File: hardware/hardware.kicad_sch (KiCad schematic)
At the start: 34 parts, among them J2 Conn_01x03, Q1 AON6500, Q2 AON6500, Q3 AON6500, Q4 AON6500, Q5 AON6500, Q6 AON6500, U1 CH32M007G8R6

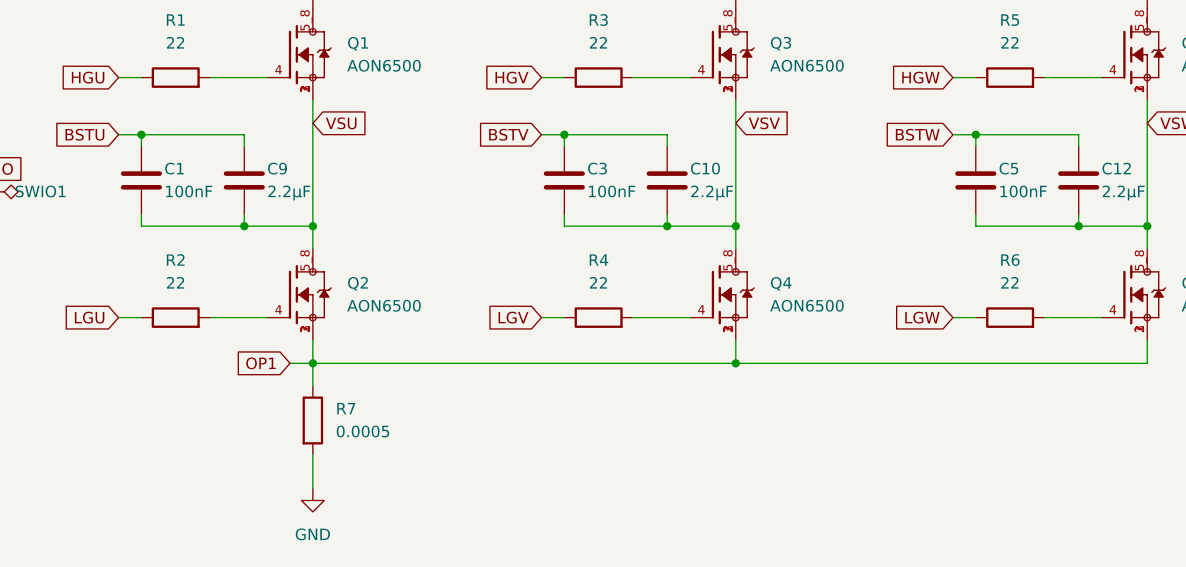
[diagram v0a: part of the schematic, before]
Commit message: change gate resistors
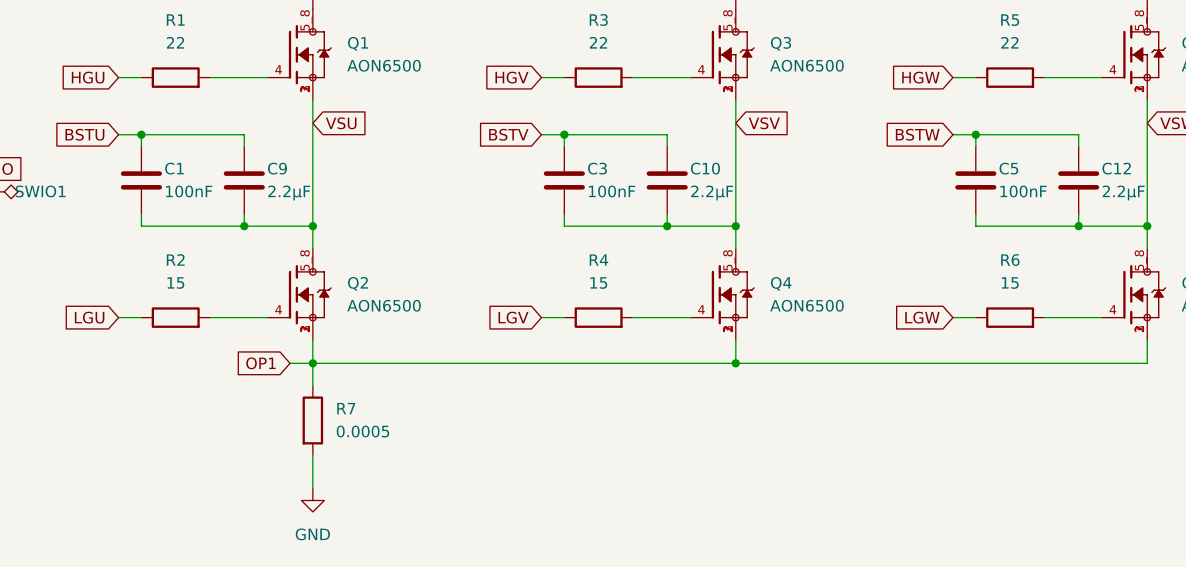
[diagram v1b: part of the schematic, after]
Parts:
- R2, R4, R6: value 22 -> 15
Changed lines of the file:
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@@
 			)
 		)
-		(property "Value" "22"
+		(property "Value" "15"
 			(at 134.62 53.34 90)
 			(show_name no)
@@
 			)
 		)
-		(property "Value" "22"
+		(property "Value" "15"
 			(at 181.61 53.34 90)
 			(show_name no)
@@
 			)
 		)
-		(property "Value" "22"
+		(property "Value" "15"
 			(at 227.33 53.34 90)
 			(show_name no)
